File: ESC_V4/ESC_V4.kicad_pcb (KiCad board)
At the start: 2 copper layers, 45 parts, among them J1 Motor Power, J2 12V Power, J3 Motor Inputs, J4 Sensor Outputs, J5 Phase A, J6 Phase B, J7 Phase C, Q1 MOSFET NPN, Q2 MOSFET NPN, Q3 MOSFET NPN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

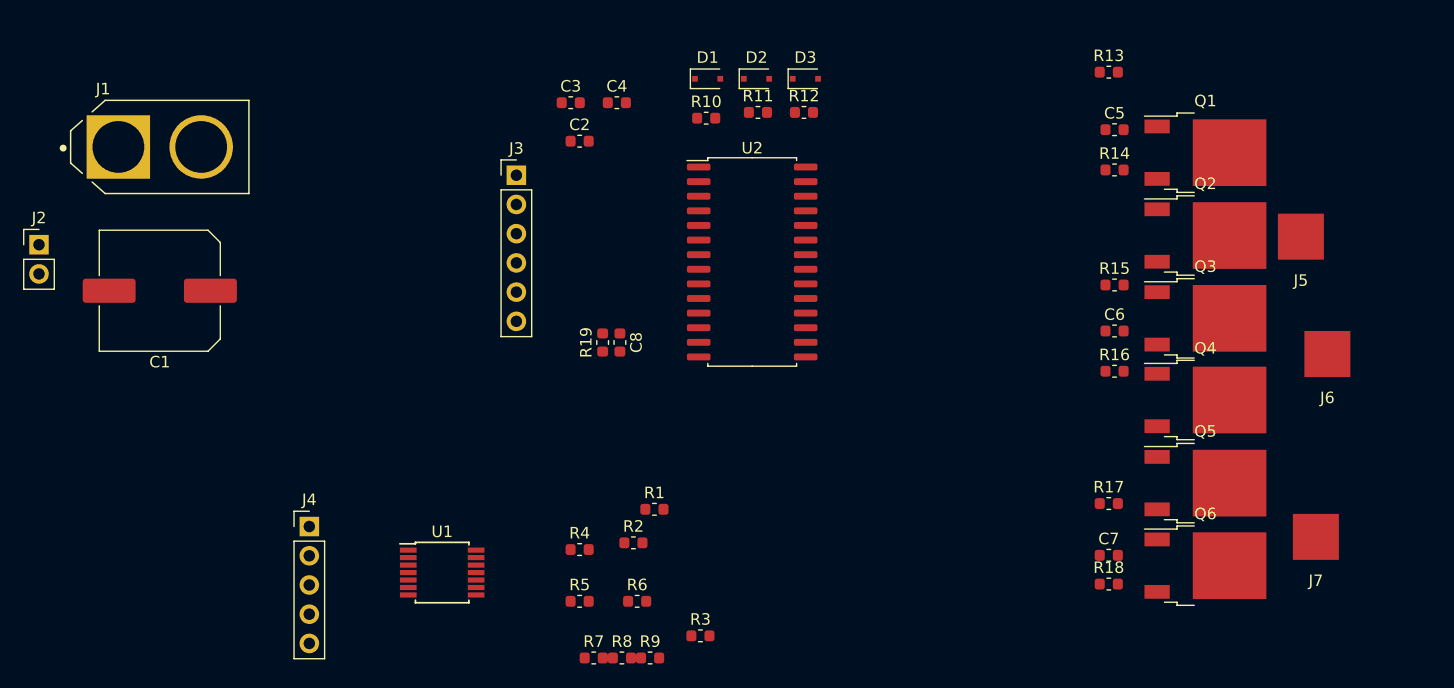
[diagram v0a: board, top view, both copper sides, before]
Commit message: Starting routing, not super happy about positions
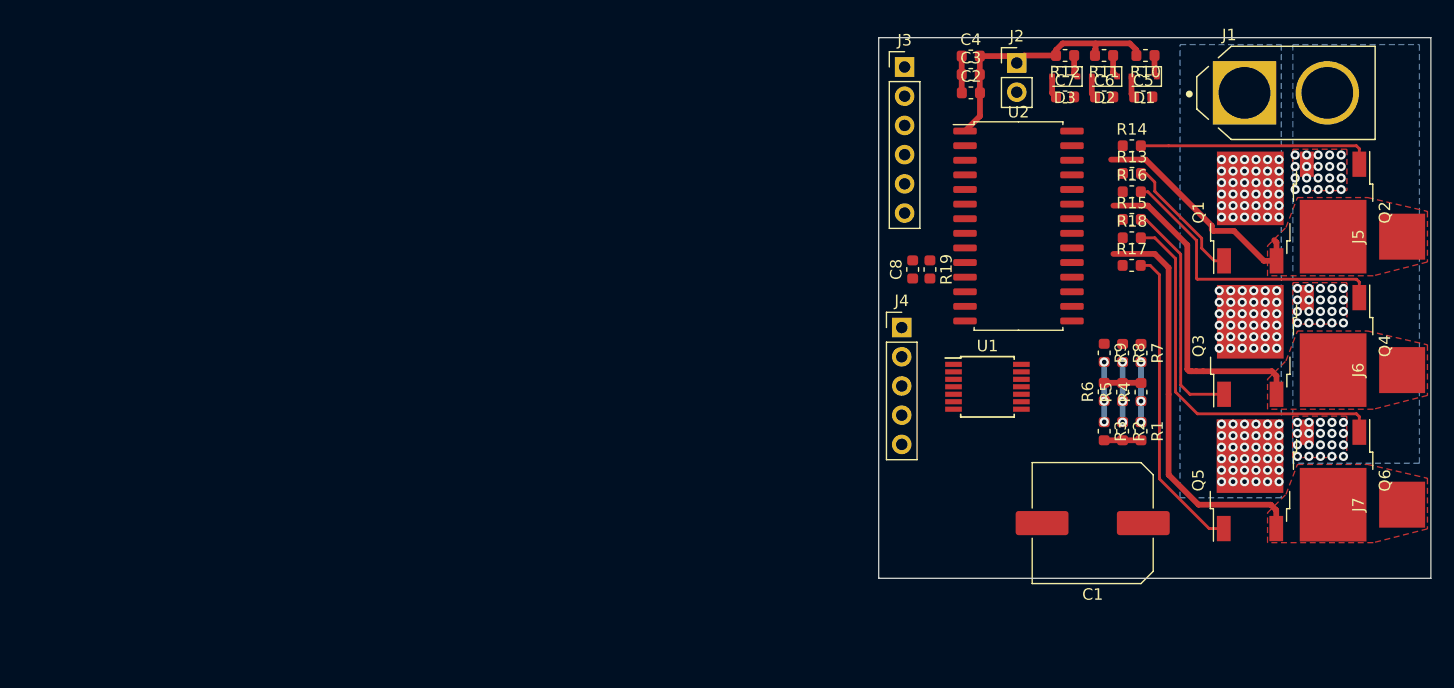
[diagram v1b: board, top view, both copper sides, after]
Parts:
- moved J1 98.0 mm to (239.4, 51.8)
- moved J2 86.5 mm to (216.0, 49.2)
- moved C1 83.6 mm to (222.6, 89.2)
- moved R7 54.5 mm to (226.8, 74.4), turned to 270 degrees
- moved J4 54.3 mm to (206.0, 72.2)
- moved R8 51.0 mm to (225.2, 74.4), turned to 270 degrees
- moved R4 50.7 mm to (226.8, 77.8), turned to 90 degrees
- moved R5 50.6 mm to (225.2, 77.8), turned to 90 degrees
- moved U1 50.1 mm to (213.4, 77.3)
- moved R9 47.6 mm to (223.6, 74.4), turned to 270 degrees
- moved R6 44.5 mm to (223.6, 77.8), turned to 90 degrees
- moved R2 43.6 mm to (225.2, 81.2), turned to 270 degrees
- moved R1 42.8 mm to (226.8, 81.2), turned to 270 degrees
- moved C7 40.0 mm to (220.2, 52.1)
- moved R3 39.3 mm to (223.6, 81.2), turned to 270 degrees
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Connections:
- C6 pad 1: FloatingSupply1 -> FloatingSupply2
- C7 pad 1: FloatingSupply1 -> FloatingSupply3
- D2 pad 2: FloatingSupply1 -> FloatingSupply2
- R17 pad 1: HO2 -> HO3
- R18 pad 1: LO2 -> LO3
- U1 pad 10: (no net) -> AnalogC
- U1 pad 11: (no net) -> GND
- U1 pad 8: (no net) -> AnalogSenseC
- U1 pad 9: (no net) -> CommonAnalog
- U2 pad 20: VB3 -> FloatingSupply3
- U2 pad 24: VB2 -> FloatingSupply2
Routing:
- net PhaseC: track 0.00 -> 36.9 mm
- net Net-(Q6-Pad1): track 0.00 -> 33.6 mm
- net PhaseB: track 0.00 -> 28.2 mm
- net Net-(Q5-Pad1): track 0.00 -> 27.1 mm
- net Net-(Q4-Pad1): track 0.00 -> 25.5 mm
- net 12V: track 0.00 -> 23.7 mm
- net Net-(Q2-Pad1): track 0.00 -> 20.4 mm
- net Net-(Q3-Pad1): track 0.00 -> 20.2 mm
- net PhaseA: track 0.00 -> 20.1 mm
- net Net-(Q1-Pad1): track 0.00 -> 11.4 mm
- net GND: track 0.00 -> 6.42 mm, vias 0 -> 60
- net AnalogB: track 0.00 -> 5.22 mm, vias 0 -> 3
- net AnalogA: track 0.00 -> 5.22 mm, vias 0 -> 3
- net AnalogC: track 0.00 -> 5.20 mm, vias 0 -> 3
- net CommonAnalog: track 0.00 -> 3.20 mm
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- added copper zone on B.Cu, net GND
- added copper zone on F.Cu, net GND
- added copper zone on F.Cu, net PhaseA
- added copper zone on F.Cu, net PhaseB
- added copper zone on F.Cu, net PhaseC
- added copper zone on B.Cu, net VMotor
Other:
- board outline added: 48 x 47 mm

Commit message: initial routing
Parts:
- moved R7 8.12 mm to (219.2, 77.3), turned to 0 degrees
- moved R3 7.65 mm to (226.4, 74.1), turned to 0 degrees
- moved R8 6.12 mm to (219.2, 75.7), turned to 0 degrees
- moved R2 5.64 mm to (226.4, 75.7), turned to 0 degrees
- moved R9 4.41 mm to (219.2, 74.1), turned to 0 degrees
- moved R1 3.93 mm to (226.4, 77.3), turned to 0 degrees
- moved R4 3.82 mm to (223.0, 77.3), turned to 180 degrees
- moved R6 3.74 mm to (223.0, 74.1), turned to 180 degrees
- moved R5 3.04 mm to (223.0, 75.7), turned to 180 degrees
- moved C1 2.53 mm to (222.2, 86.7), turned to 90 degrees
- moved R19 1.77 mm to (206.7, 66.9)
- moved C8 1.47 mm to (208.4, 66.9)
- moved U1 1.20 mm to (212.2, 77.3), turned to 90 degrees
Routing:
- net GND: track 6.42 -> 89.2 mm, vias 60 -> 70
- net PhaseA: track 20.1 -> 62.0 mm, vias 0 -> 2
- net PhaseB: track 28.2 -> 66.1 mm, vias 0 -> 2
- net PhaseC: track 36.9 -> 68.5 mm, vias 0 -> 1
- net CommonAnalog: track 3.20 -> 28.4 mm, vias 0 -> 3
- net LO3: track 0.00 -> 18.5 mm, vias 0 -> 3
- net FloatingSupply3: track 1.91 -> 19.6 mm, vias 0 -> 2
- net LO1: track 0.00 -> 17.4 mm, vias 0 -> 2
- net 12V: track 23.7 -> 40.6 mm, vias 0 -> 2
- net LO2: track 0.00 -> 15.3 mm, vias 0 -> 2
- net 5V: track 0.00 -> 15.1 mm
- net AnalogB: track 5.22 -> 18.1 mm, vias 3 -> 4
- net AnalogSenseC: track 0.00 -> 12.5 mm, vias 0 -> 2
- net AnalogA: track 5.22 -> 17.0 mm, vias 3 -> 4
- net AnalogC: track 5.20 -> 15.8 mm, vias 3 -> 4
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
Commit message: Fix enable connection
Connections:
- U2 pad 10: Enable -> 5V
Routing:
- net 5V: track 15.1 -> 24.0 mm, vias 0 -> 1

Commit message: Potentially finished layout
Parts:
- moved J3 0.25 mm to (206.0, 49.5)
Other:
- board text added: "12V"
- board text added: "5V"
- board text added: "A"
- board text added: "AA"
- board text added: "AB"
- board text added: "AC"
- board text added: "B"
- board text added: "C"
- board text added: "ESC V4 Colin Snow 5/5/22 The List"
- board text added: "GND"
- board text added: "H1"
- board text added: "H2"
- board text added: "H3"
- board text added: "L1"
- board text added: "L2"
- board text added: "L3"
- board text added: "VIN"

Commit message: Potentially finished board
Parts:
- added G***: LOGO, Components:NoFire2, B.Cu at (230.8, 74.9)
- added G***: LOGO, Components:FDLogo3, F.Cu at (210.0, 91.2)
- moved R3 8.80 mm to (218.4, 77.7), turned to 180 degrees
- moved R1 8.50 mm to (218.4, 74.5), turned to 180 degrees
- moved R2 8.03 mm to (218.4, 76.1), turned to 180 degrees
- moved R9 7.34 mm to (225.6, 77.7), turned to 180 degrees
- moved R7 6.96 mm to (225.6, 74.5), turned to 180 degrees
- moved R8 6.39 mm to (225.6, 76.1), turned to 180 degrees
- moved R6 3.79 mm to (221.8, 77.7), turned to 0 degrees
- moved R4 3.06 mm to (221.8, 74.5), turned to 0 degrees
- moved R5 1.29 mm to (221.8, 76.1), turned to 0 degrees
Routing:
- net PhaseA: track 62.0 -> 49.5 mm
- net PhaseB: track 66.1 -> 54.2 mm
- net CommonAnalog: track 28.4 -> 19.1 mm
- net GND: track 89.2 -> 94.9 mm
- net PhaseC: track 68.5 -> 64.0 mm, vias 1 -> 2
- net AnalogC: track 15.8 -> 19.3 mm, vias 4 -> 5
- net AnalogA: track 17.0 -> 19.1 mm, vias 4 -> 6
- net LogicalLow3: track 5.45 -> 6.40 mm
- net AnalogB: track 18.1 -> 17.4 mm
